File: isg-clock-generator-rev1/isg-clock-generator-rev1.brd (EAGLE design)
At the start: 76.2 x 76.2 mm, 160 parts, among them IC1 LMK03318RHSR, IC4 TPS7A8001DRBR, IC5 TPS7A8001DRBR, Q1 7M50072001, X1 OUT2_P, X2 OUT2_N, X3 OUT0_P, X4 PRIREF_P, X5 PRIREF_N, X6 V_IN_EXT

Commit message: More routing, decaps and config headers
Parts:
- moved C55 70.5 mm to (73.0, 33.3), turned to 0 degrees
- moved C56 69.5 mm to (73.0, 30.8), turned to 0 degrees
- moved C57 68.8 mm to (73.0, 28.3), turned to 0 degrees
- moved JP10 60.4 mm to (8.89, 22.2), turned to 180 degrees
- moved JP8 60.4 mm to (8.89, 15.9), turned to 180 degrees
- moved JP9 60.4 mm to (8.89, 19.1), turned to 180 degrees
- moved JP12 57.0 mm to (66.7, 30.8), turned to 90 degrees
- moved R40 47.8 mm to (15.2, 19.1), turned to 90 degrees
- moved R43 47.8 mm to (15.2, 22.2), turned to 270 degrees
- moved R39 46.1 mm to (17.0, 15.9)
- moved R41 43.3 mm to (17.0, 19.1), turned to 270 degrees
- moved R44 43.3 mm to (17.0, 22.2), turned to 90 degrees
- moved R42 39.0 mm to (18.7, 19.1), turned to 90 degrees
- moved R45 39.0 mm to (18.7, 22.2), turned to 270 degrees
- moved C58 33.9 mm to (49.7, 29.1), turned to 0 degrees
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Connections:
- net N$24 renamed GPIO4_JUMPER
- net N$25 renamed GPIO3_JUMPER
- net N$26 renamed GPIO0_JUMPER
- net N$27 renamed GPIO2_JUMPER
- net N$28 renamed HWCTRL_JUMPER
- net N$29 renamed GPIO1_JUMPER
- net N$31 renamed REFSEL_JUMPER
- net N$4 renamed PULLUP_GPIO5
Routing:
- net GPIO2: track 0.00 -> 28.1 mm
- net GPIO5: track 17.8 -> 45.2 mm
- net GPIO1: track 0.00 -> 26.1 mm
- net GPIO3: track 0.00 -> 25.7 mm
- net GPIO4: track 0.00 -> 22.8 mm
- net HW_SW_CTRL: track 0.00 -> 21.3 mm
- net REFSEL: track 0.00 -> 20.8 mm
- net LF_R: track 9.44 -> 20.3 mm
- net PULLUP_GPIO5: track 0.00 -> 9.59 mm
- net PP_P3V3_PLL_CORE: track 6.98 -> 16.4 mm, vias 0 -> 8
- net GPIO1_JUMPER: track 0.00 -> 8.83 mm
- net GPIO4_JUMPER: track 0.00 -> 8.79 mm
- net GPIO3_JUMPER: track 0.00 -> 8.79 mm
- net GPIO2_JUMPER: track 0.00 -> 8.79 mm
- net GPIO0_JUMPER: track 0.00 -> 8.69 mm
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- added copper zone on layer 15, net PP_P1V8_VDDO
- added copper zone on layer 15, net PP_P3V3_PLL_CORE
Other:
- board text added: "FRAC-N"
- board text added: "INT-N"
- board text added: "NARROW"

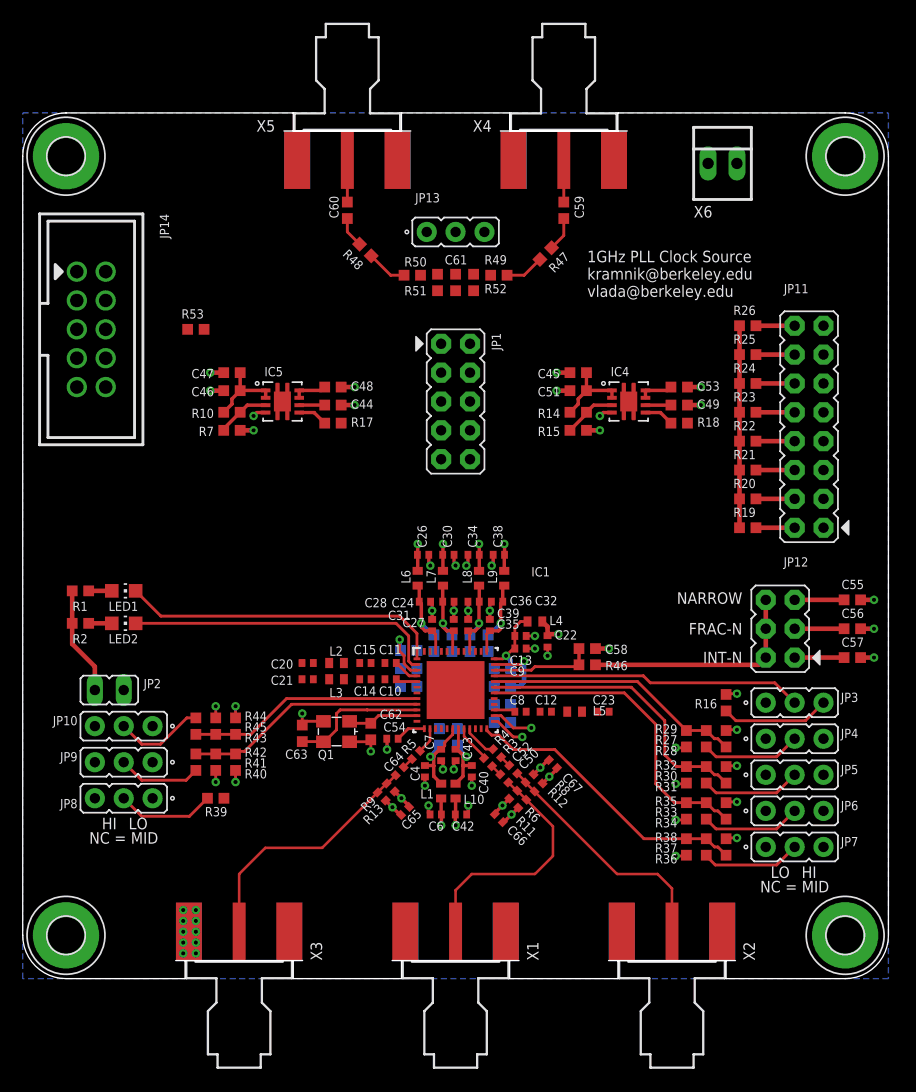
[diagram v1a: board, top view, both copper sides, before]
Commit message: Preliminary connections made to PRIREF inputs
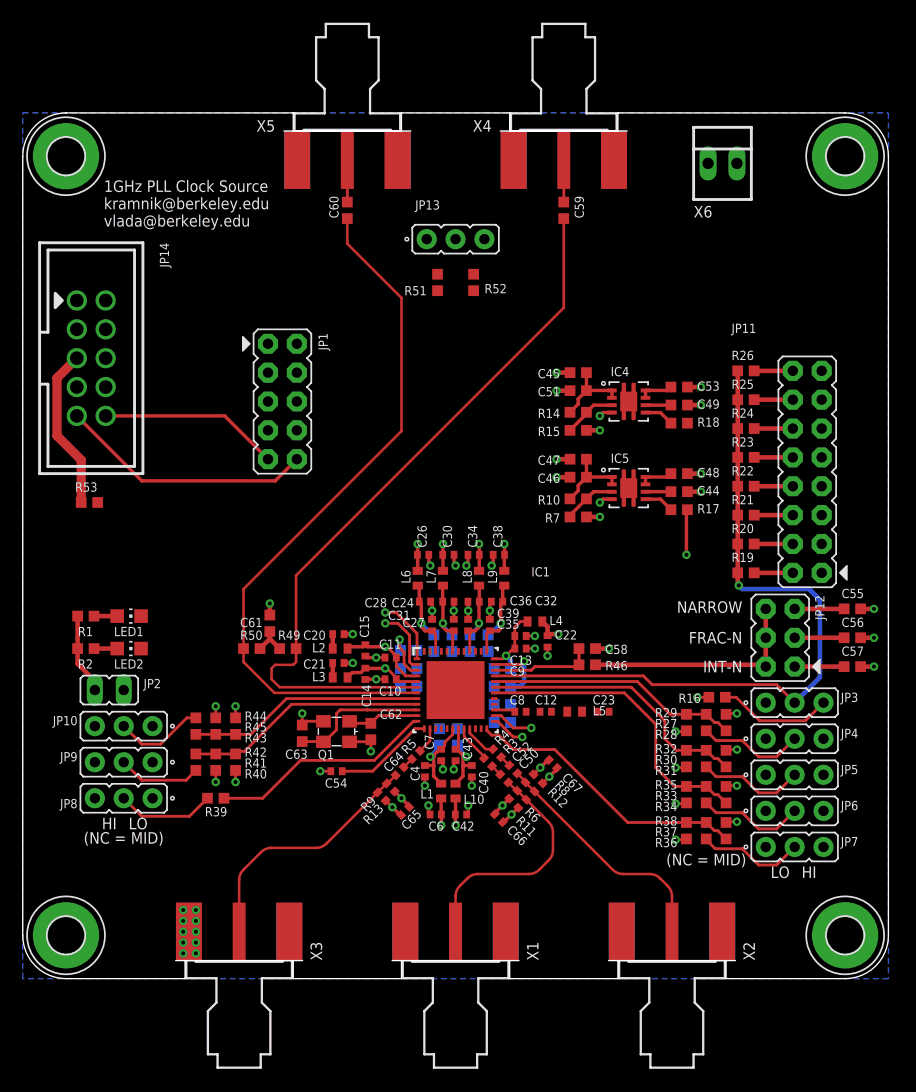
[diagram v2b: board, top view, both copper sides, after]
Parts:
- removed R47, R48: 0R JUMPER 0603, rcl-modified-footprints:R0603
- moved R49 37.7 mm to (23.3, 29.1)
- moved R50 35.8 mm to (20.2, 29.1)
- moved C61 34.2 mm to (21.7, 31.3), turned to 90 degrees
- moved C46 31.4 mm to (48.9, 44.1)
- moved C47 31.4 mm to (48.9, 45.7)
- moved IC5 31.4 mm to (53.3, 43.2)
- moved R10 31.4 mm to (48.9, 42.2)
- moved R7 31.4 mm to (48.9, 40.6)
- moved C44 31.4 mm to (57.8, 42.9)
- moved C48 31.4 mm to (57.8, 44.5)
- moved R17 31.4 mm to (57.8, 41.3)
- moved R53 17.9 mm to (5.87, 41.9)
- moved JP1 15.2 mm to (22.9, 50.8)
- moved C54 5.69 mm to (27.6, 18.3)
- moved JP11 3.97 mm to (69.1, 44.6)
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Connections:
- removed net PRIREF_RC_N: C60.1, X5.1
- removed net PRIREF_RC_P: C59.1, X4.1
- net PRIREF_N: now also C60.2; no longer R48.1
- net PRIREF_P: now also C59.2; no longer R47.1
- net PRIREF_R_N: now also C60.1, X5.1; no longer C60.2, R48.2
- net PRIREF_R_P: now also C59.1, X4.1; no longer C59.2, R47.2
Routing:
- net PRIREF_P: track 3.47 -> 65.2 mm
- net PRIREF_N: track 3.60 -> 63.2 mm
- net STATUS0: track 28.5 -> 5.79 mm, vias 0 -> 1
- net SCL: track 3.72 -> 26.2 mm
- net STATUS1: track 27.6 -> 5.69 mm, vias 0 -> 1
- net GPIO0: track 0.00 -> 19.8 mm
- net GPIO5: track 45.2 -> 64.0 mm, vias 0 -> 1
- net SDA: track 3.04 -> 18.9 mm
- net N$6: track 0.00 -> 14.3 mm
- net PP_P3V3_PLL_CORE: track 16.4 -> 23.0 mm, vias 8 -> 9
- net PDN: track 2.67 -> 8.78 mm
- net GND: track 55.7 -> 61.8 mm, vias 55 -> 60
- net VDD_DIG: track 2.28 -> 7.93 mm, vias 0 -> 1
- net VDD_IN: track 1.90 -> 7.02 mm, vias 0 -> 1
- net PRIREF_RC_P: track 3.69 -> 0.00 mm
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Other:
- board text added: "(NC = MID)"
- board text removed: "NC = MID"

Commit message: Close to done, VIN still unconnected and TPS needs package fixed
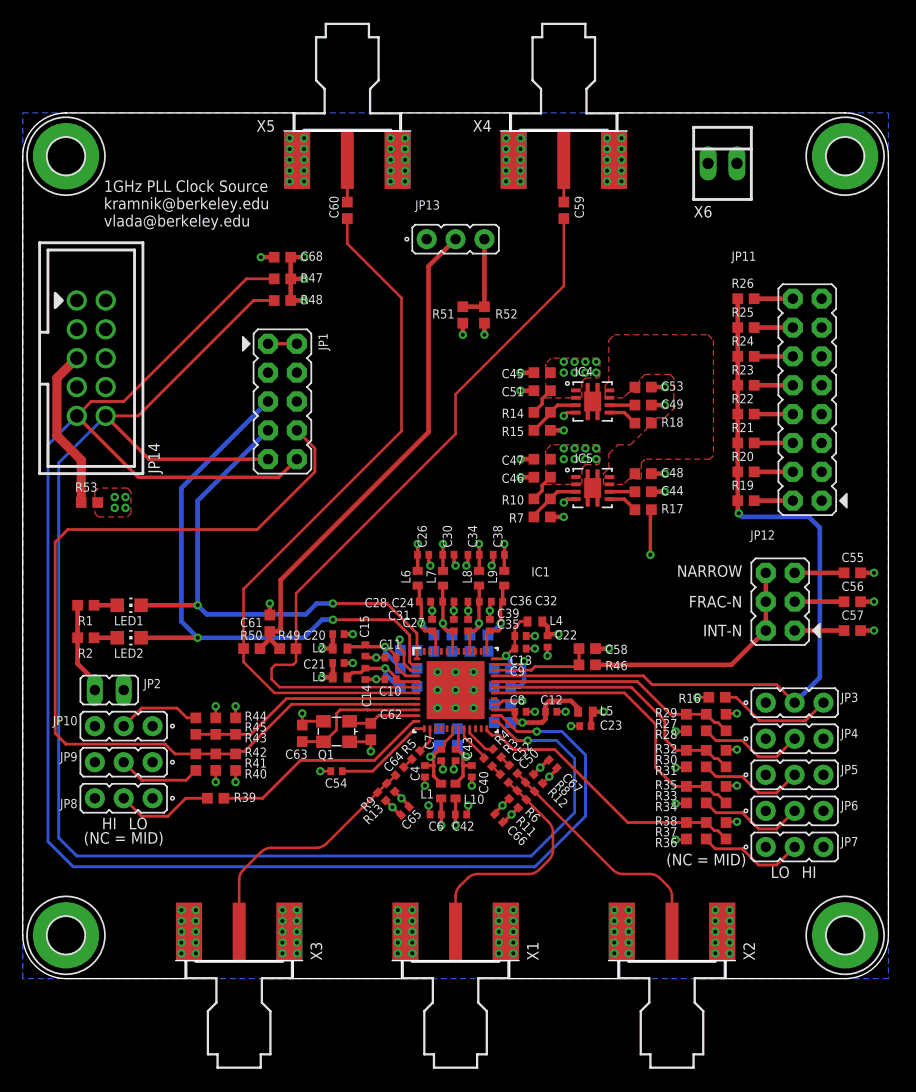
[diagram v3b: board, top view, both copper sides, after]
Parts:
- added C68: CAP CER 0.1UF 25V X7R 0603 10%, rcl-modified-footprints:C0603
- added R47, R48: RES SMD 1K OHM 1% 1/10W 0603, rcl-modified-footprints:R0603
- JP14: value CON_OST_302-S101 -> TI USB2ANY
- moved JP11 6.35 mm to (69.1, 51.0)
- moved R19 6.35 mm to (63.7, 42.1)
- moved R20 6.35 mm to (63.7, 44.6)
- moved R21 6.35 mm to (63.7, 47.1)
- moved R22 6.35 mm to (63.7, 49.7)
- moved R23 6.35 mm to (63.7, 52.2)
- moved R25 6.35 mm to (63.7, 57.3)
- moved R26 6.35 mm to (63.7, 59.8)
- moved R24 6.35 mm to (63.7, 54.8)
- moved R51 3.62 mm to (38.7, 58.4)
- moved C45 3.18 mm to (45.7, 53.3)
- moved C46 3.18 mm to (45.7, 44.1)
- moved C47 3.18 mm to (45.7, 45.7)
- moved C51 3.18 mm to (45.7, 51.8)
- moved IC4 3.18 mm to (50.2, 50.8)
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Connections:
- net N$5 renamed PRIREF_VCM_DIVIDER
- net N$6 renamed EXT_VDD
- net GND: now also C68.2
- net PP_P3V3_PLL_CORE: now also C68.1, R47.2, R48.2
- net SCL: now also R47.1
- net SDA: now also R48.1
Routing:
- net SCL: track 26.2 -> 148.1 mm
- net SDA: track 18.9 -> 134.6 mm
- net HW_SW_CTRL: track 21.3 -> 81.0 mm
- net STATUS1: track 5.69 -> 52.5 mm, vias 1 -> 2
- net PRIREF_VCM: track 3.07 -> 44.8 mm
- net STATUS0: track 5.79 -> 46.3 mm, vias 1 -> 2
- net GND: track 61.8 -> 83.2 mm, vias 60 -> 164
- net VDD_LDO: track 1.88 -> 11.3 mm, vias 0 -> 1
- net PP_P3V3_PLL_CORE: track 23.0 -> 31.1 mm, vias 9 -> 28
- net PRIREF_VCM_DIVIDER: track 0.00 -> 7.85 mm
- net GPIO5: track 64.0 -> 70.3 mm
- net PP_P1V8_VDDO: track 27.0 -> 22.6 mm, vias 9 -> 17
- net DECAP_LDO: track 0.00 -> 3.75 mm, vias 0 -> 1
- net VIN: track 6.03 -> 3.37 mm
- net VDD_DIG: track 7.93 -> 10.4 mm
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- added copper zone on layer 1, net PP_P1V8_VDDO
- added copper zone on layer 1, net PP_P3V3_PLL_CORE
- added copper zone on layer 1, net VIN

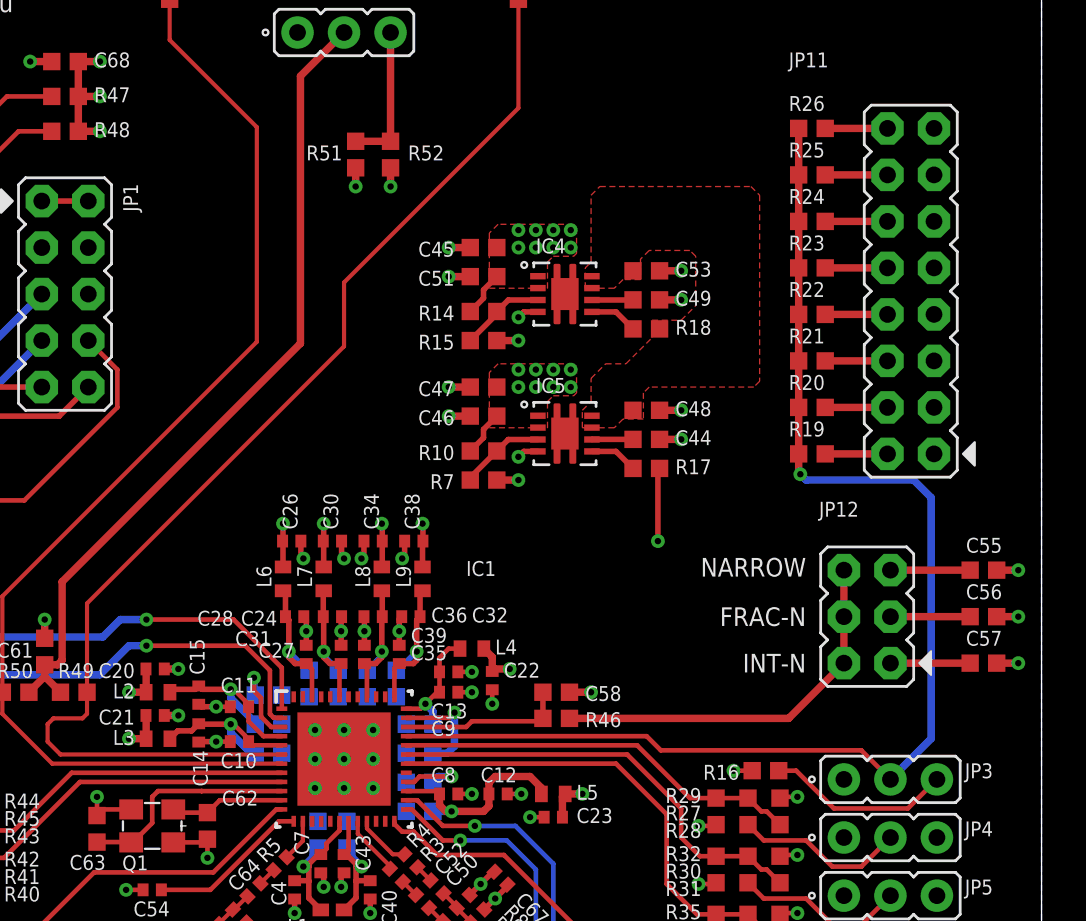
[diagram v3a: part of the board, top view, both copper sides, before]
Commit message: Fixed TPS landing pattern
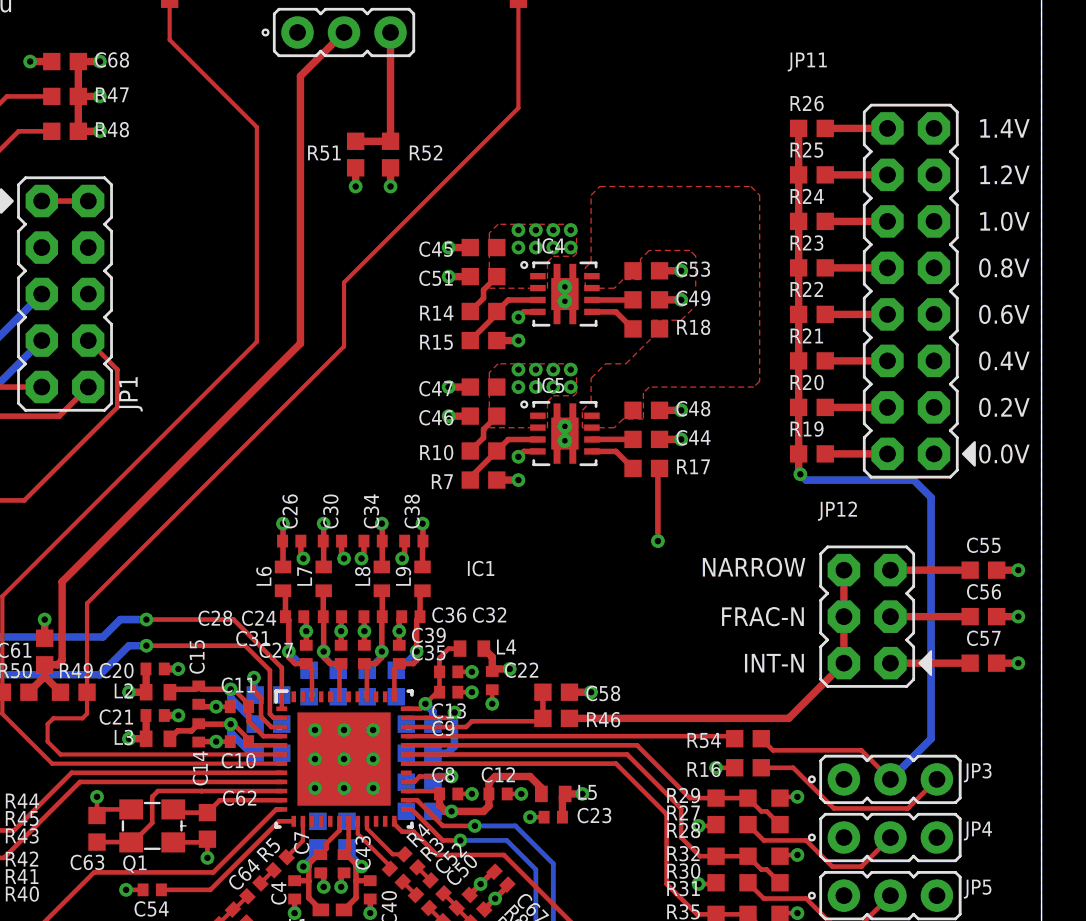
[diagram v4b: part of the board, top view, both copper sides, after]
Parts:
- added R54: 0R JUMPER 0603, rcl-modified-footprints:R0603
- C50, C52, C64: value 0R JUMPER -> 0R JUMPER 0402
- JP1: value MOTHERBOARD -> EOS_MOTHERBOARD
- JP14: value TI USB2ANY -> TI_USB2ANY
- R3, R4, R5: value 0R JUMPER 0603 -> 0R JUMPER 0402
- moved R16 0.97 mm to (60.2, 24.9)
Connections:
- new net GPIO5_JUMPER: JP3.2, R19.1, R20.1, R21.1, R22.1, R23.1, R24.1, R25.1, R26.1, R54.2
- net GND: now also IC4.PAD, IC4.PAD1, IC4.PAD2, IC4.PAD3, IC4.PAD4, IC4.VIA1, IC4.VIA2, IC5.PAD, IC5.PAD1, IC5.PAD2, IC5.PAD3, IC5.PAD4, IC5.VIA1, IC5.VIA2; no longer IC4.9, IC5.9
- net GPIO5: now also R54.1; no longer JP3.2, R19.1, R20.1, R21.1, R22.1, R23.1, R24.1, R25.1, R26.1
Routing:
- net GPIO5: track 70.3 -> 18.0 mm, vias 1 -> 0
- net GPIO5_JUMPER: track 0.00 -> 50.9 mm, vias 0 -> 1
- net GND: track 83.2 -> 91.2 mm
- net PULLUP_GPIO5: track 10.2 -> 11.2 mm
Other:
- board text added: "0.0V"
- board text added: "0.2V"
- board text added: "0.4V"
- board text added: "0.6V"
- board text added: "0.8V"
- board text added: "1.0V"
- board text added: "1.2V"
- board text added: "1.4V"

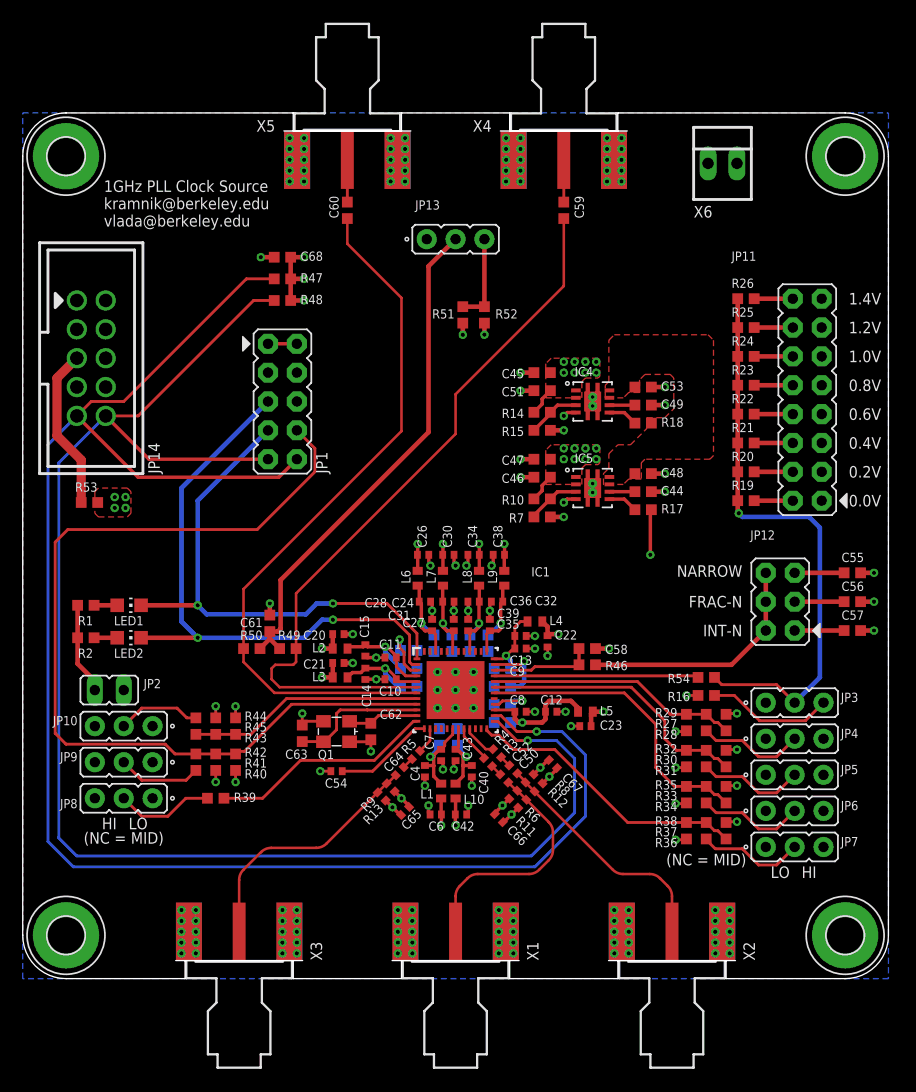
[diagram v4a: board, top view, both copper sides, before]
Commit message: First-pass routing done
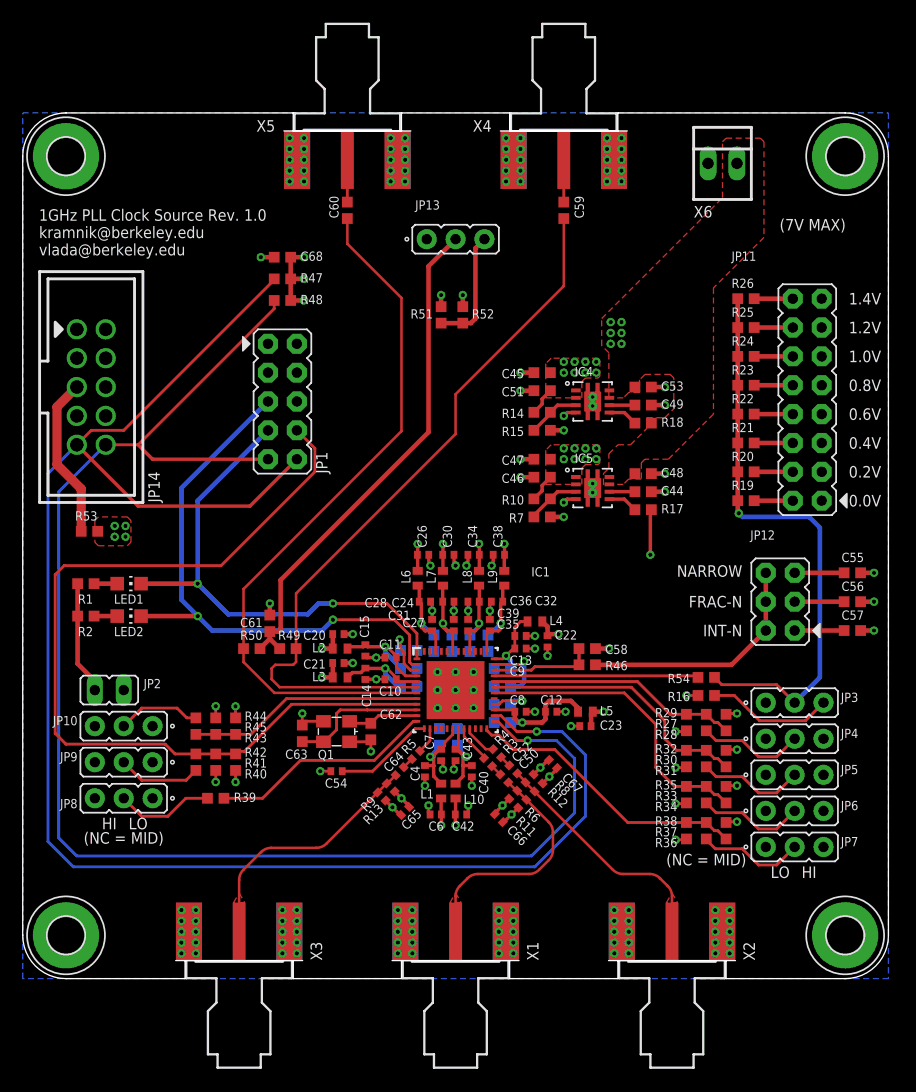
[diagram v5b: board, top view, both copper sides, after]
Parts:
- moved JP14 2.54 mm to (6.03, 52.1)
- moved R53 2.54 mm to (5.87, 39.4)
- moved LED1 1.91 mm to (9.37, 34.8)
- moved LED2 1.91 mm to (9.37, 31.9)
- moved R1 1.91 mm to (5.56, 34.8)
- moved R2 1.91 mm to (5.56, 31.9)
- moved R51 1.91 mm to (36.8, 58.4), turned to 90 degrees
- moved R52 1.91 mm to (38.7, 58.4), turned to 270 degrees
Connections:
- net GND: now also X6.1
- net VIN: now also X6.2
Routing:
- net SDA: track 134.6 -> 129.6 mm
- net PRIREF_VCM_DIVIDER: track 7.85 -> 10.5 mm
- net VIN: track 3.37 -> 0.83 mm, vias 0 -> 6
- net STATUS_LED_PWR: track 8.09 -> 10.00 mm
- net HW_SW_CTRL: track 81.0 -> 79.3 mm
- net STATUS1: track 52.5 -> 50.9 mm
- net STATUS0: track 46.3 -> 45.2 mm
- net GND: track 91.2 -> 92.0 mm
- added copper zone on layer 1, net OUT0_R_C_P
- added copper zone on layer 1, net OUT2_R_C_N
- added copper zone on layer 1, net OUT2_R_C_P
- added copper zone on layer 15, net VIN
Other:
- board text added: "(7V MAX)"
- board text added: "1GHz PLL Clock Source Rev. 1.0 kramnik@berkeley.edu vlada@berkeley.edu"
- board text removed: "1GHz PLL Clock Source kramnik@berkeley.edu vlada@berkeley.edu"
